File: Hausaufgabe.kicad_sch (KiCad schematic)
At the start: 20 parts, among them Q1 Q_Dual_NPN_NPN_E1B1C2E2B2C1, Q2 Q_Dual_NPN_NPN_E1B1C2E2B2C1, SW1 SW_SPST

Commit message: comment about change
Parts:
- D1, D2, D3, D4, D5, D6: footprint LED_SMD:LED_1206_3216Metric_ReverseMount_Hole1.8x2.4mm -> Custom reverse mount LED:custom reverse mount LED
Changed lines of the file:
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@@
     (property "Reference" "D3" (id 0) (at 88.9 49.53 0))
     (property "Value" "LED" (id 1) (at 88.9 52.07 0))
-    (property "Footprint" "LED_SMD:LED_1206_3216Metric_ReverseMount_Hole1.8x2.4mm" (id 2) (at 88.9 55.88 0)
+    (property "Footprint" "Custom reverse mount LED:custom reverse mount LED" (id 2) (at 88.9 55.88 0)
       (effects (font (size 1.27 1.27)) hide)
     )
@@
     (property "Reference" "D4" (id 0) (at 88.9 69.85 0))
     (property "Value" "LED" (id 1) (at 88.9 72.39 0))
-    (property "Footprint" "LED_SMD:LED_1206_3216Metric_ReverseMount_Hole1.8x2.4mm" (id 2) (at 88.9 76.2 0)
+    (property "Footprint" "Custom reverse mount LED:custom reverse mount LED" (id 2) (at 88.9 76.2 0)
       (effects (font (size 1.27 1.27)) hide)
     )
@@
     (property "Reference" "D5" (id 0) (at 88.9 90.17 0))
     (property "Value" "LED" (id 1) (at 88.9 92.71 0))
-    (property "Footprint" "LED_SMD:LED_1206_3216Metric_ReverseMount_Hole1.8x2.4mm" (id 2) (at 88.9 96.52 0)
+    (property "Footprint" "Custom reverse mount LED:custom reverse mount LED" (id 2) (at 88.9 96.52 0)
       (effects (font (size 1.27 1.27)) hide)
     )
@@
     (property "Reference" "D6" (id 0) (at 88.9 110.49 0))
     (property "Value" "LED" (id 1) (at 88.9 113.03 0))
-    (property "Footprint" "LED_SMD:LED_1206_3216Metric_ReverseMount_Hole1.8x2.4mm" (id 2) (at 88.9 116.84 0)
+    (property "Footprint" "Custom reverse mount LED:custom reverse mount LED" (id 2) (at 88.9 116.84 0)
       (effects (font (size 1.27 1.27)) hide)
     )
@@
       (effects (font (size 1.27 1.27)) (justify right))
     )
-    (property "Footprint" "LED_SMD:LED_1206_3216Metric_ReverseMount_Hole1.8x2.4mm" (id 2) (at 187.96 88.9 0)
+    (property "Footprint" "Custom reverse mount LED:custom reverse mount LED" (id 2) (at 187.96 88.9 0)
       (effects (font (size 1.27 1.27)) hide)
     )
@@
       (effects (font (size 1.27 1.27)) (justify right))
     )
-    (property "Footprint" "LED_SMD:LED_1206_3216Metric_ReverseMount_Hole1.8x2.4mm" (id 2) (at 248.92 91.44 0)
+    (property "Footprint" "Custom reverse mount LED:custom reverse mount LED" (id 2) (at 248.92 91.44 0)
       (effects (font (size 1.27 1.27)) hide)
     )
@@
     )
     (path "/a5e62cad-9913-400e-811e-dd54e35a9202"
-      (reference "D1") (unit 1) (value "LED") (footprint "LED_SMD:LED_1206_3216Metric_ReverseMount_Hole1.8x2.4mm")
+      (reference "D1") (unit 1) (value "LED") (footprint "Custom reverse mount LED:custom reverse mount LED")
     )
     (path "/350d8671-112c-413c-906b-7e5b7d111766"
-      (reference "D2") (unit 1) (value "LED") (footprint "LED_SMD:LED_1206_3216Metric_ReverseMount_Hole1.8x2.4mm")
+      (reference "D2") (unit 1) (value "LED") (footprint "Custom reverse mount LED:custom reverse mount LED")
     )
     (path "/263cea63-ee65-4ba3-aabc-bd6dde217a5d"
-      (reference "D3") (unit 1) (value "LED") (footprint "LED_SMD:LED_1206_3216Metric_ReverseMount_Hole1.8x2.4mm")
+      (reference "D3") (unit 1) (value "LED") (footprint "Custom reverse mount LED:custom reverse mount LED")
     )
     (path "/c08f0bc3-2471-421d-b8ec-090d4a56f807"
-      (reference "D4") (unit 1) (value "LED") (footprint "LED_SMD:LED_1206_3216Metric_ReverseMount_Hole1.8x2.4mm")
+      (reference "D4") (unit 1) (value "LED") (footprint "Custom reverse mount LED:custom reverse mount LED")
     )
     (path "/efab3e9e-eaab-4794-9f1a-a2e79832933f"
-      (reference "D5") (unit 1) (value "LED") (footprint "LED_SMD:LED_1206_3216Metric_ReverseMount_Hole1.8x2.4mm")
+      (reference "D5") (unit 1) (value "LED") (footprint "Custom reverse mount LED:custom reverse mount LED")
     )
     (path "/13a231e9-030b-487a-8a2d-b532535bae2f"
-      (reference "D6") (unit 1) (value "LED") (footprint "LED_SMD:LED_1206_3216Metric_ReverseMount_Hole1.8x2.4mm")
+      (reference "D6") (unit 1) (value "LED") (footprint "Custom reverse mount LED:custom reverse mount LED")
     )
     (path "/9e90674f-a5a3-4e72-8998-9c8445be783f"

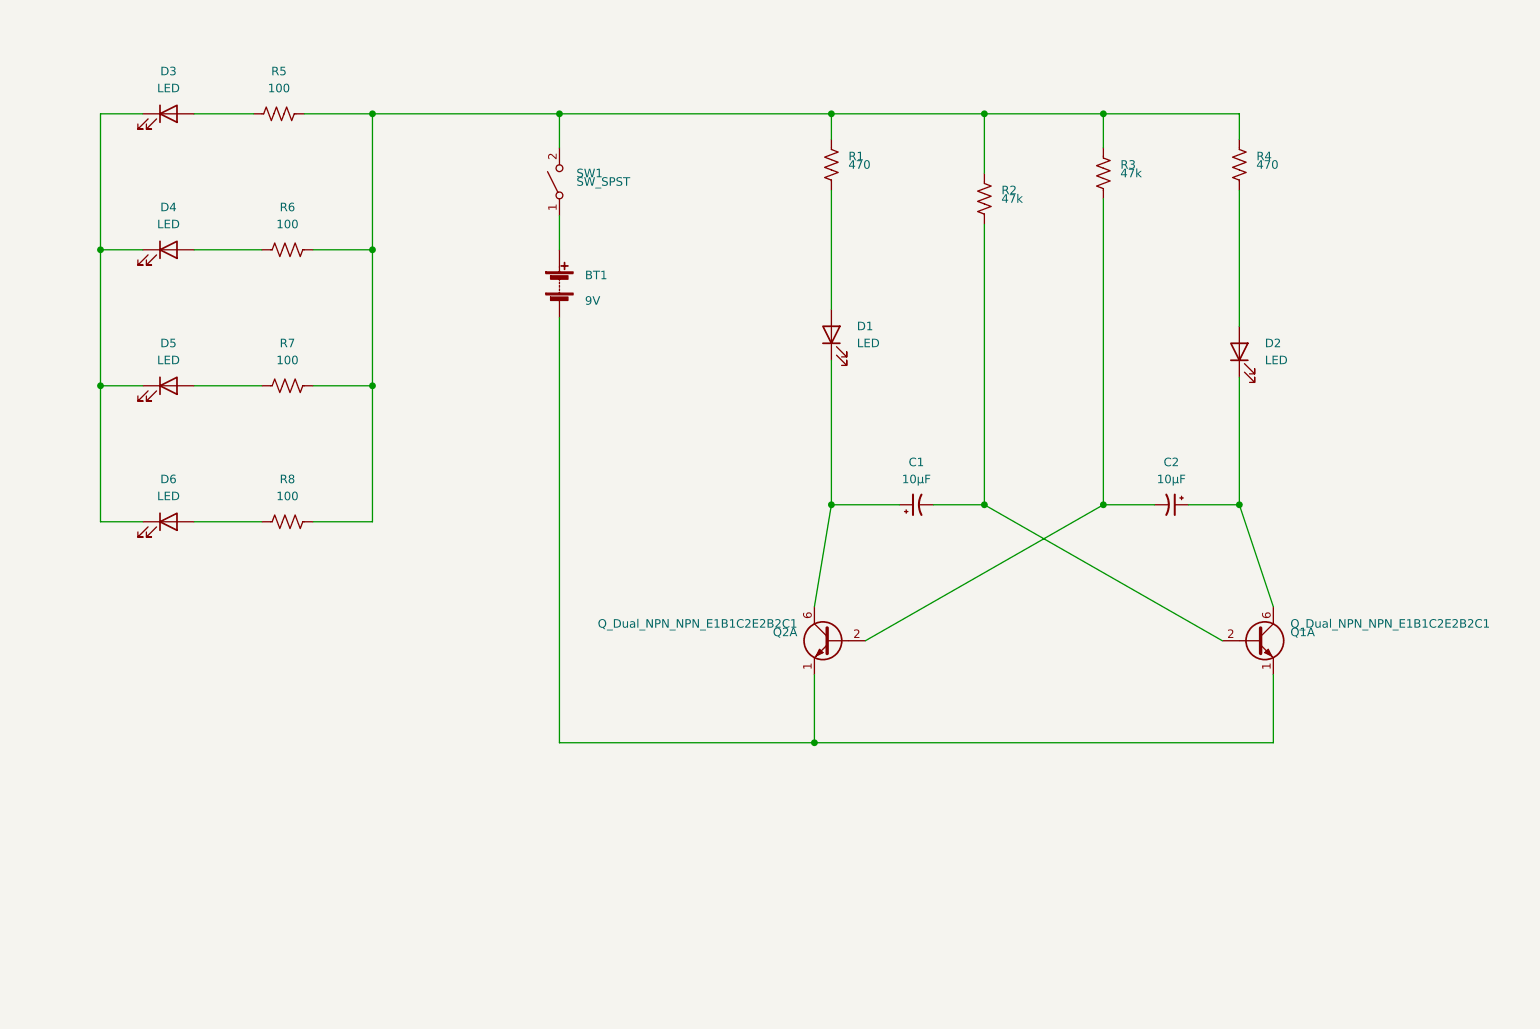
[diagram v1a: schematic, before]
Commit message: fixed footprint and routing
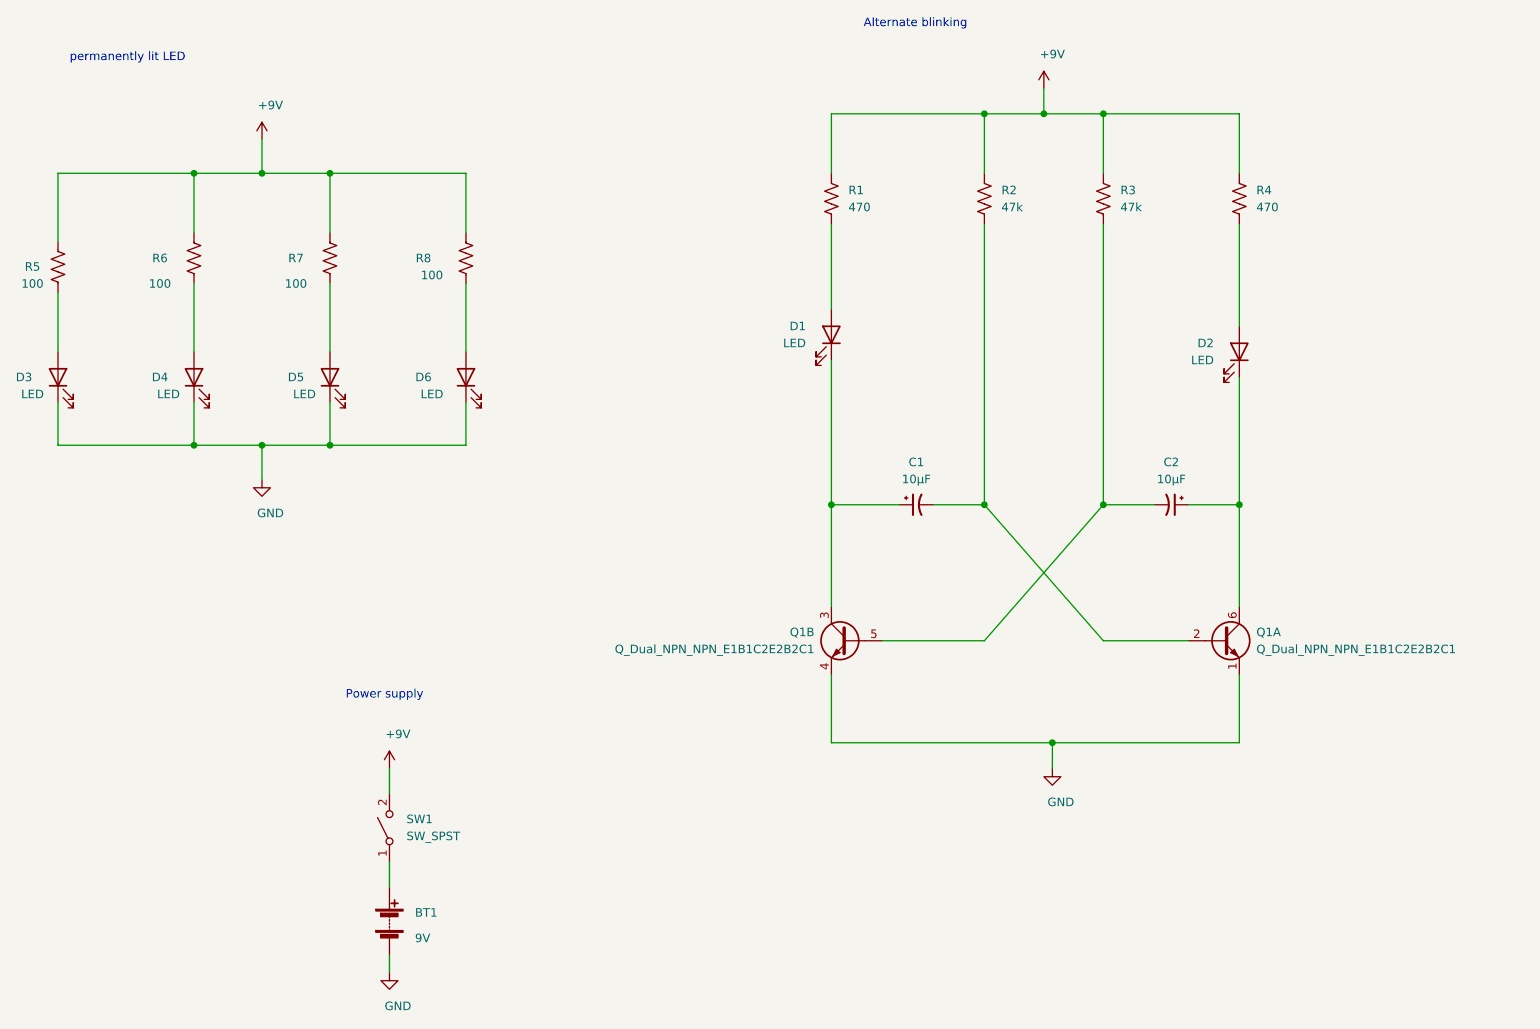
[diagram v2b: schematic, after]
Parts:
- removed Q2: Q_Dual_NPN_NPN_E1B1C2E2B2C1, Package_TO_SOT_SMD:SOT-23_Handsoldering, symbol Device:Q_Dual_NPN_NPN_E1B1C2E2B2C1
- added unit 2 of Q1
- Q1: footprint Package_TO_SOT_SMD:SOT-23_Handsoldering -> Package_TO_SOT_SMD:SOT-363_SC-70-6_Handsoldering
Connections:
- net +9V: now reaches R1.1, R2.1, R3.1, R4.1, R5.2, R6.2, R7.2, R8.2, SW1.2 (B)
- net GND: now reaches BT1.2 (-), Q1.1 (E1)
- net GND: now also D3.1 (K), D4.1 (K), D5.1 (K), D6.1 (K), Q1.4 (E2)
- net at C2.2, R3.2: now also Q1.5 (B2)
- net at C1.1, D1.1 (K): now also Q1.3 (C2)
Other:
- note added: "Alternate blinking"
- note added: "Power supply"
- note added: "permanently lit LED"
- moved on the sheet: BT1, D1, D2, D3, D4, D5, D6, R1, R3, R4, R5, R6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

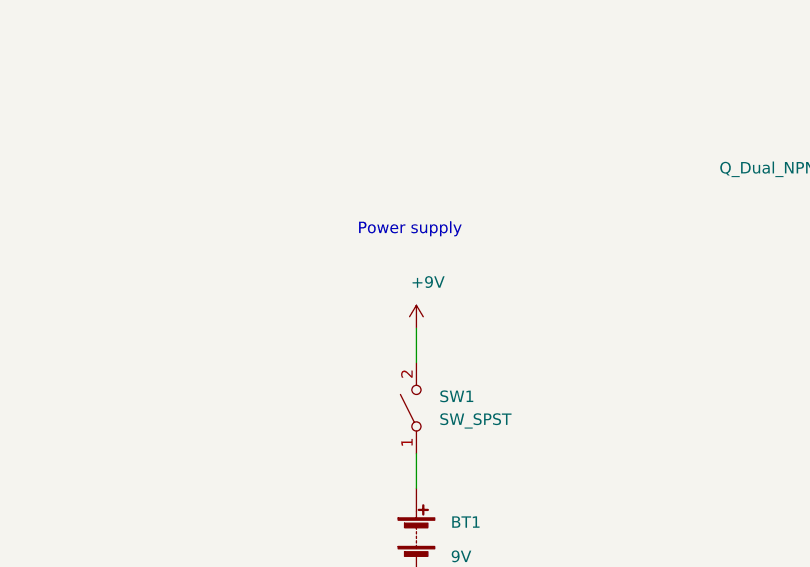
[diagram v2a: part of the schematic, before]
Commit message: changed LED and switch footprint, cleaned up frontside of board
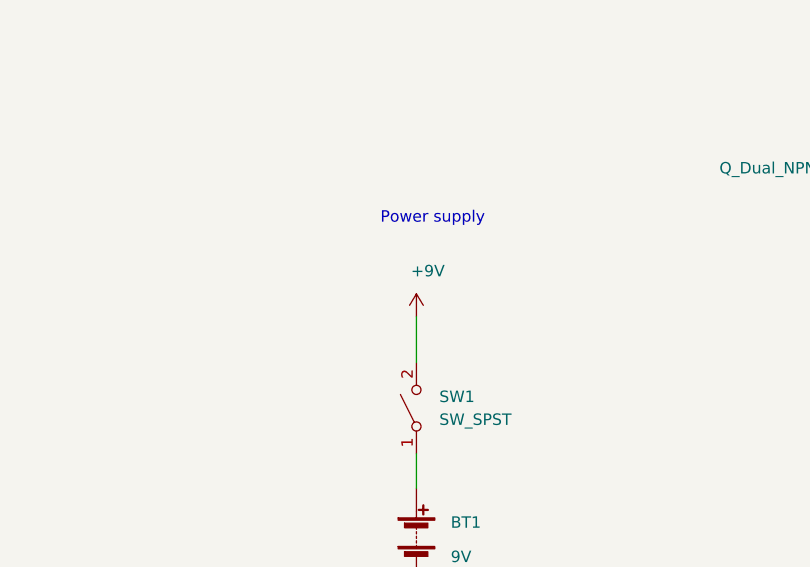
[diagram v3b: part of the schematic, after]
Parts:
- D1, D2, D3, D4, D5, D6: footprint Custom reverse mount LED:custom reverse mount LED -> Custom reverse mount LED:custom_reverse_mount_LED
- SW1: footprint Button_Switch_SMD:SW_DIP_SPSTx01_Slide_6.7x4.1mm_W6.73mm_P2.54mm_LowProfile_JPin -> Custom Slider Switch:CL-SB-22B
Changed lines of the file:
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@@
     (stroke (width 0) (type solid) (color 0 0 0 0))
   )
-  (wire (pts (xy 121.92 153.67) (xy 121.92 157.48))
+  (wire (pts (xy 121.92 152.4) (xy 121.92 157.48))
     (stroke (width 0) (type solid) (color 0 0 0 0))
   )
@@
     (effects (font (size 1.27 1.27)) (justify right bottom))
   )
-  (text "Power supply" (at 127 143.51 180)
+  (text "Power supply" (at 129.54 142.24 180)
     (effects (font (size 1.27 1.27)) (justify right bottom))
   )
@@
     )
   )
-  (symbol (lib_id "power:+9V") (at 121.92 153.67 0) (unit 1)
+  (symbol (lib_id "power:+9V") (at 121.92 152.4 0) (unit 1)
     (in_bom yes) (on_board yes)
-    (property "Reference" "#PWR0105" (id 0) (at 121.92 157.48 0)
+    (property "Reference" "#PWR0105" (id 0) (at 121.92 156.21 0)
       (effects (font (size 1.27 1.27)) hide)
     )
-    (property "Value" "+9V" (id 1) (at 123.19 148.59 0))
-    (property "Footprint" "" (id 2) (at 121.92 153.67 0)
+    (property "Value" "+9V" (id 1) (at 123.19 147.32 0))
+    (property "Footprint" "" (id 2) (at 121.92 152.4 0)
       (effects (font (size 1.27 1.27)) hide)
     )
-    (property "Datasheet" "" (id 3) (at 121.92 153.67 0)
+    (property "Datasheet" "" (id 3) (at 121.92 152.4 0)
       (effects (font (size 1.27 1.27)) hide)
     )
@@
     (property "Reference" "D3" (id 0) (at 67.31 95.25 90))
     (property "Value" "LED" (id 1) (at 68.58 97.79 90))
-    (property "Footprint" "Custom reverse mount LED:custom reverse mount LED" (id 2) (at 72.39 95.25 0)
+    (property "Footprint" "Custom reverse mount LED:custom_reverse_mount_LED" (id 2) (at 72.39 95.25 0)
       (effects (font (size 1.27 1.27)) hide)
     )
@@
     (property "Reference" "D4" (id 0) (at 87.63 95.25 90))
     (property "Value" "LED" (id 1) (at 88.9 97.79 90))
-    (property "Footprint" "Custom reverse mount LED:custom reverse mount LED" (id 2) (at 92.71 95.25 0)
+    (property "Footprint" "Custom reverse mount LED:custom_reverse_mount_LED" (id 2) (at 92.71 95.25 0)
       (effects (font (size 1.27 1.27)) hide)
     )
@@
     (property "Reference" "D5" (id 0) (at 107.95 95.25 90))
     (property "Value" "LED" (id 1) (at 109.22 97.79 90))
-    (property "Footprint" "Custom reverse mount LED:custom reverse mount LED" (id 2) (at 113.03 95.25 0)
+    (property "Footprint" "Custom reverse mount LED:custom_reverse_mount_LED" (id 2) (at 113.03 95.25 0)
       (effects (font (size 1.27 1.27)) hide)
     )
@@
     (property "Reference" "D6" (id 0) (at 127 95.25 90))
     (property "Value" "LED" (id 1) (at 128.27 97.79 90))
-    (property "Footprint" "Custom reverse mount LED:custom reverse mount LED" (id 2) (at 133.35 95.25 0)
+    (property "Footprint" "Custom reverse mount LED:custom_reverse_mount_LED" (id 2) (at 133.35 95.25 0)
       (effects (font (size 1.27 1.27)) hide)
     )
@@
       (effects (font (size 1.27 1.27)) (justify right))
     )
-    (property "Footprint" "Custom reverse mount LED:custom reverse mount LED" (id 2) (at 187.96 88.9 0)
+    (property "Footprint" "Custom reverse mount LED:custom_reverse_mount_LED" (id 2) (at 187.96 88.9 0)
       (effects (font (size 1.27 1.27)) hide)
     )
@@
       (effects (font (size 1.27 1.27)) (justify right))
     )
-    (property "Footprint" "Custom reverse mount LED:custom reverse mount LED" (id 2) (at 248.92 91.44 0)
+    (property "Footprint" "Custom reverse mount LED:custom_reverse_mount_LED" (id 2) (at 248.92 91.44 0)
       (effects (font (size 1.27 1.27)) hide)
     )
@@
       (effects (font (size 1.27 1.27)) (justify right))
     )
-    (property "Footprint" "Button_Switch_SMD:SW_DIP_SPSTx01_Slide_6.7x4.1mm_W6.73mm_P2.54mm_LowProfile_JPin" (id 2) (at 121.92 162.56 0)
+    (property "Footprint" "Custom Slider Switch:CL-SB-22B" (id 2) (at 121.92 162.56 0)
       (effects (font (size 1.27 1.27)) hide)
     )
@@
     )
     (path "/a5e62cad-9913-400e-811e-dd54e35a9202"
-      (reference "D1") (unit 1) (value "LED") (footprint "Custom reverse mount LED:custom reverse mount LED")
+      (reference "D1") (unit 1) (value "LED") (footprint "Custom reverse mount LED:custom_reverse_mount_LED")
     )
     (path "/350d8671-112c-413c-906b-7e5b7d111766"
-      (reference "D2") (unit 1) (value "LED") (footprint "Custom reverse mount LED:custom reverse mount LED")
+      (reference "D2") (unit 1) (value "LED") (footprint "Custom reverse mount LED:custom_reverse_mount_LED")
     )
     (path "/263cea63-ee65-4ba3-aabc-bd6dde217a5d"
-      (reference "D3") (unit 1) (value "LED") (footprint "Custom reverse mount LED:custom reverse mount LED")
+      (reference "D3") (unit 1) (value "LED") (footprint "Custom reverse mount LED:custom_reverse_mount_LED")
     )
     (path "/c08f0bc3-2471-421d-b8ec-090d4a56f807"
-      (reference "D4") (unit 1) (value "LED") (footprint "Custom reverse mount LED:custom reverse mount LED")
+      (reference "D4") (unit 1) (value "LED") (footprint "Custom reverse mount LED:custom_reverse_mount_LED")
     )
     (path "/efab3e9e-eaab-4794-9f1a-a2e79832933f"
-      (reference "D5") (unit 1) (value "LED") (footprint "Custom reverse mount LED:custom reverse mount LED")
+      (reference "D5") (unit 1) (value "LED") (footprint "Custom reverse mount LED:custom_reverse_mount_LED")
     )
     (path "/13a231e9-030b-487a-8a2d-b532535bae2f"
-      (reference "D6") (unit 1) (value "LED") (footprint "Custom reverse mount LED:custom reverse mount LED")
+      (reference "D6") (unit 1) (value "LED") (footprint "Custom reverse mount LED:custom_reverse_mount_LED")
     )
     (path "/c0d52315-383f-4615-83bc-c90aef30d1d9"
@@
       (reference "R8") (unit 1) (value "100") (footprint "Resistor_SMD:R_0805_2012Metric_Pad1.20x1.40mm_HandSolder")
     )
-    (path "/d48d9f66-8193-42d8-b975-91991045ee28"
-      (reference "SW1") (unit 1) (value "SW_SPST") (footprint "Button_Switch_SMD:SW_DIP_SPSTx01_Slide_6.7x4.1mm_W6.73mm_P2.54mm_LowProfile_JPin")
+    (path "/f374b93e-6dbd-45c4-a9d3-6773792bd36a"
+      (reference "SW1") (unit 1) (value "SW_SPST") (footprint "Custom Slider Switch:CL-SB-22B")
     )
   )
